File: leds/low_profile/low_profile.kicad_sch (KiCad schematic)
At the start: 14 parts, among them J2 428202214

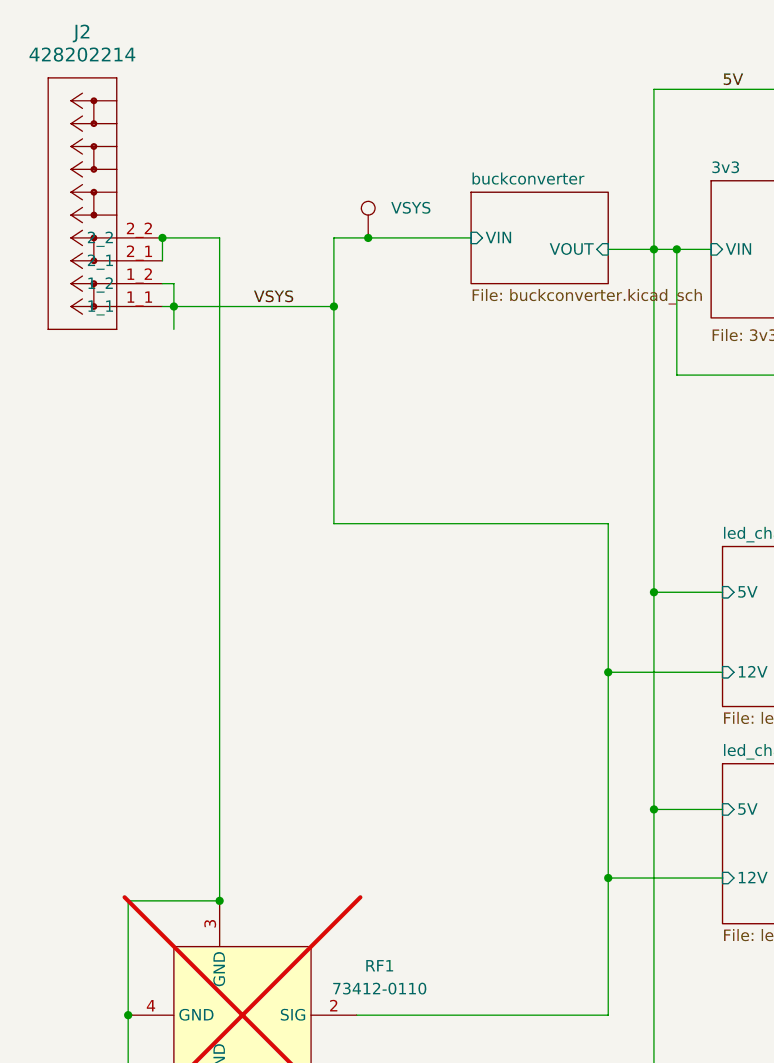
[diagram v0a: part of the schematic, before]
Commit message: Low profile LED controller
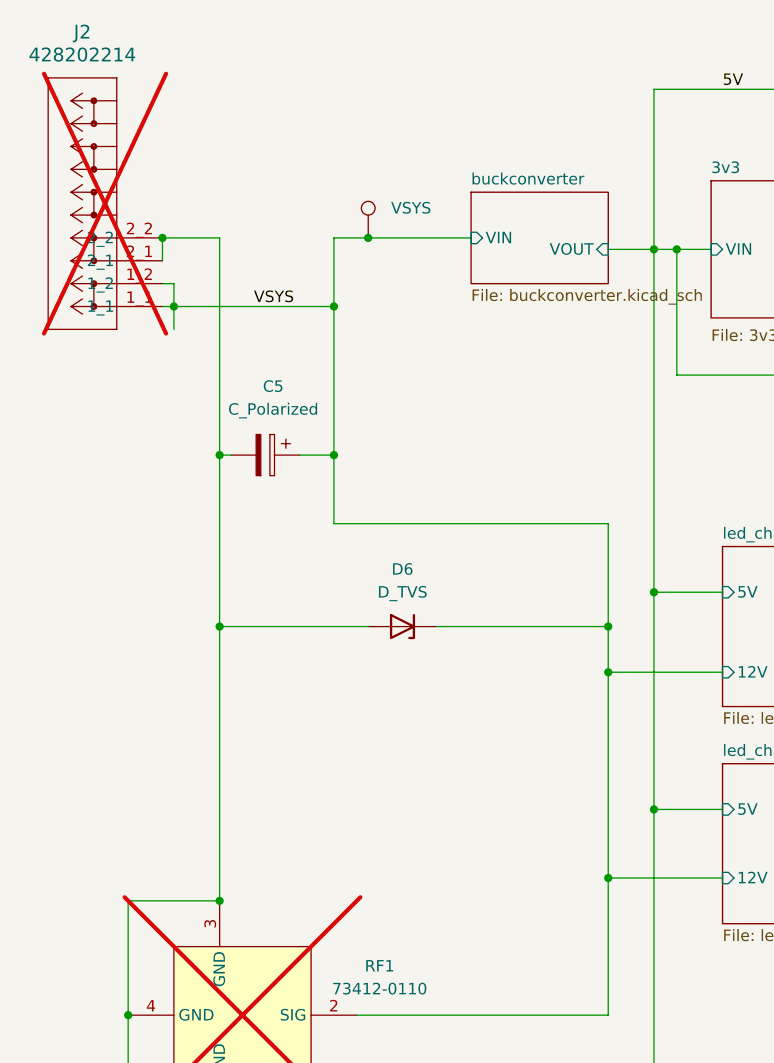
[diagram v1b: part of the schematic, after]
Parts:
- added C5: C_Polarized, Capacitor_SMD:CP_Elec_8x11.9, symbol Device:C_Polarized
- added D6: D_TVS, Diode_SMD:D_SMB, symbol Device:D_Zener
- J2: now not fitted; now left out of the parts list
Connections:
- net GND: now also C5.2, D6.2 (A)
- net VSYS: now also C5.1, D6.1 (K)
